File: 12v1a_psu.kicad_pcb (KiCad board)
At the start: 2 copper layers, 130 x 100 mm, 24 parts, among them J1 AC_in, J2 P1, J3 P2, J4 Vout, Q1 BD440, SW1 SW_SPST, U1 LM7812

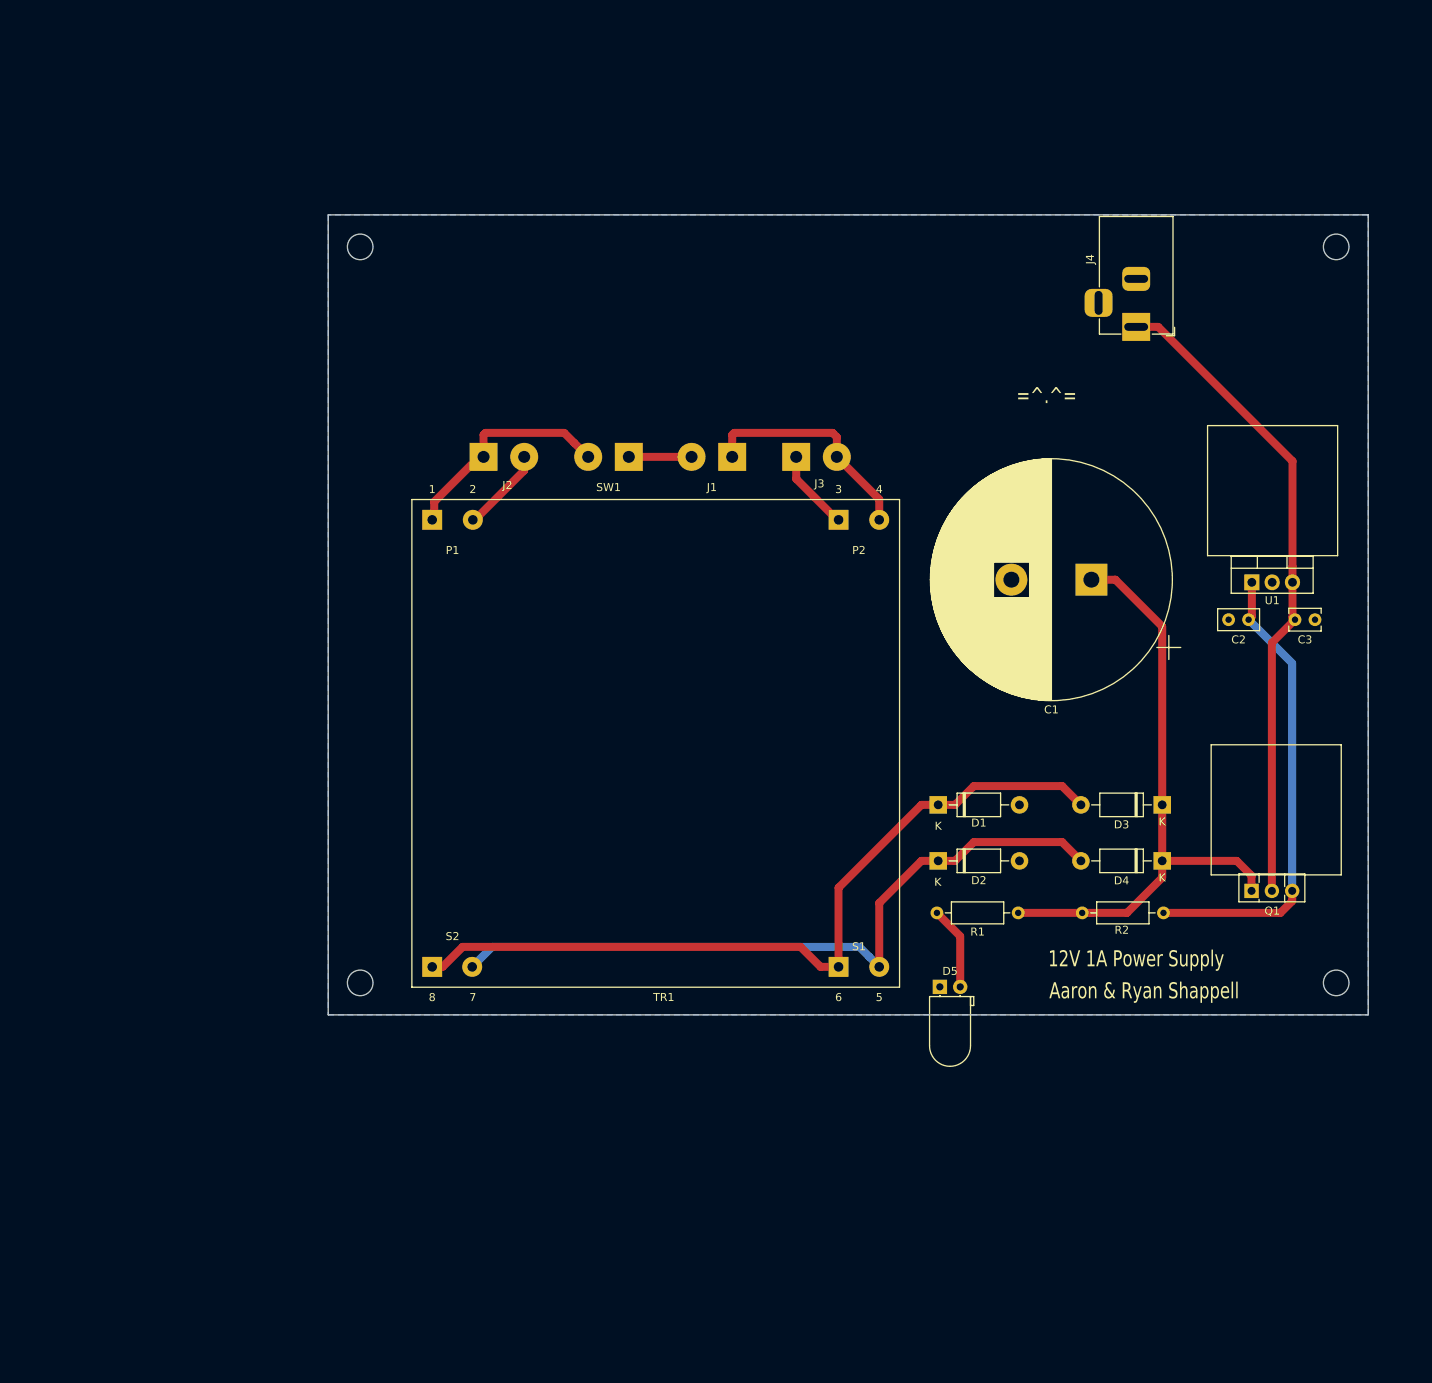
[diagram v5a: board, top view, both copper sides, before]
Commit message: Chose bjt for reg, picked footprints
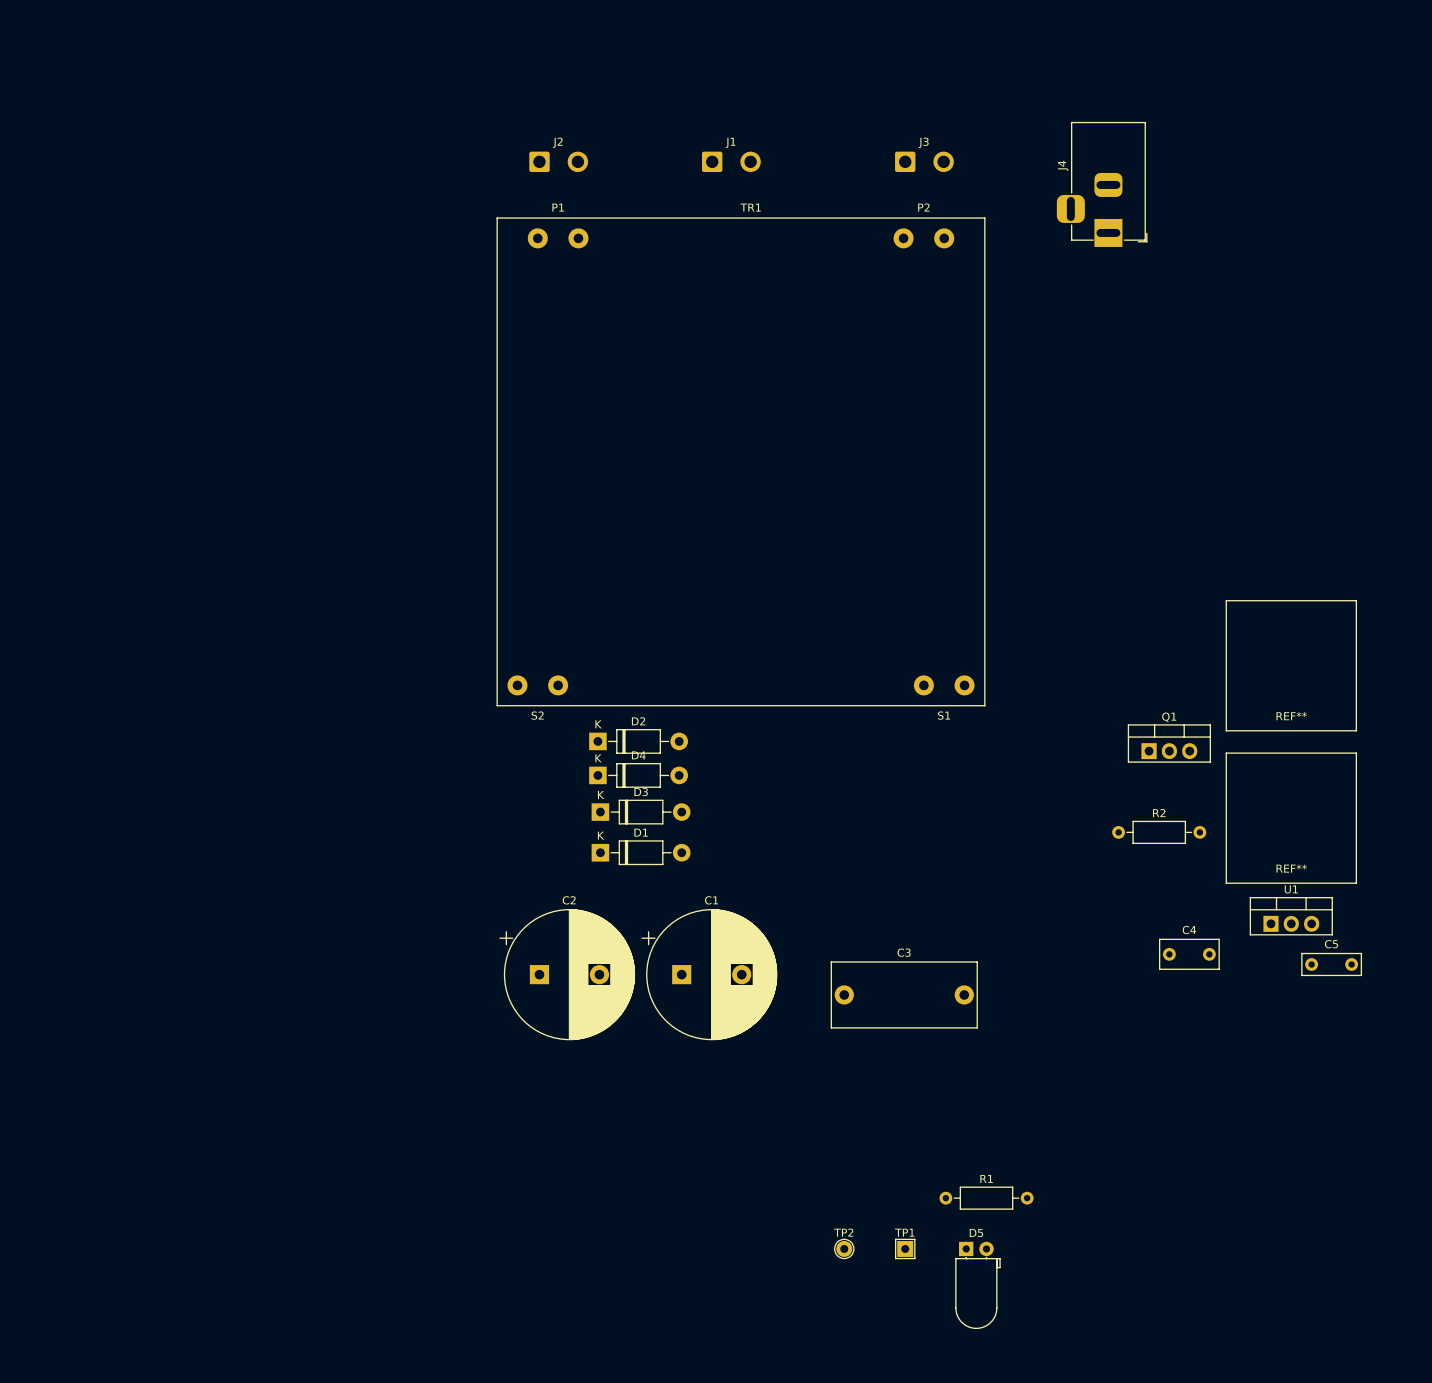
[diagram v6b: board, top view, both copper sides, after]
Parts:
- removed the REF** at (83.0, 142.0)
- removed the REF** at (205.0, 50.0)
- removed the REF** at (205.0, 142.0)
- removed the REF** at (83.0, 50.0)
- removed the REF** at (197.1, 88.6)
- removed the REF** at (197.5, 128.5)
- removed SW1: SW_SPST, Connector_Wire:SolderWirePad_1x02_P5.08mm_Drill1.5mm
- added C4: 0.33u, Capacitor_THT:C_Rect_L7.2mm_W3.5mm_P5.00mm_FKS2_FKP2_MKS2_MKP2, F.Cu at (184.2, 138.4)
- added C5: 0.1u, Capacitor_THT:C_Rect_L7.2mm_W2.5mm_P5.00mm_FKS2_FKP2_MKS2_MKP2, F.Cu at (201.9, 139.7)
- added REF**: Heatsink, 12v1a_psu:Heatsink, F.Cu at (199.4, 129.5)
- added REF**: Heatsink, 12v1a_psu:Heatsink, F.Cu at (199.4, 110.5)
- added TP1: TestPoint, TestPoint:TestPoint_THTPad_2.0x2.0mm_Drill1.0mm, F.Cu at (151.1, 175.3)
- added TP2: TestPoint, TestPoint:TestPoint_THTPad_D2.0mm_Drill1.0mm, F.Cu at (143.5, 175.3)
- C1: value 10000u -> 2200u; footprint Capacitor_THT:CP_Radial_D30.0mm_P10.00mm_SnapIn -> Capacitor_THT:CP_Radial_D16.0mm_P7.50mm
- C2: value 0.33u -> 2200u; footprint Capacitor_THT:C_Disc_D5.0mm_W2.5mm_P2.50mm -> Capacitor_THT:CP_Radial_D16.0mm_P7.50mm
- C3: value 0.1u -> 1u; footprint Capacitor_THT:C_Disc_D3.8mm_W2.6mm_P2.50mm -> Capacitor_THT:C_Rect_L18.0mm_W8.0mm_P15.00mm_FKS3_FKP3
- J1: value AC_in -> AC_IN; footprint Connector_Wire:SolderWirePad_1x02_P5.08mm_Drill1.5mm -> Connector_Wire:SolderWire-0.75sqmm_1x02_P4.8mm_D1.25mm_OD2.3mm
- J2, J3: footprint Connector_Wire:SolderWirePad_1x02_P5.08mm_Drill1.5mm -> Connector_Wire:SolderWire-0.75sqmm_1x02_P4.8mm_D1.25mm_OD2.3mm
- J4: footprint Connector_BarrelJack:BarrelJack_Horizontal -> 12v1a_psu:BarrelJack_Horizontal
- Q1: value BD440 -> TIP32AG; footprint Package_TO_SOT_THT:TO-126-3_Vertical -> Package_TO_SOT_THT:TO-220-3_Vertical
- TR1: footprint L01-6353:Transformer_L01-6353 -> 12v1a_psu:L01-6363
- U1: value LM7812 -> L7812
- moved C2 99.1 mm to (105.4, 141.0), turned to 0 degrees
- moved TR1 74.0 mm to (130.6, 76.9)
- moved C3 73.3 mm to (143.5, 143.5)
- moved D4 71.3 mm to (112.7, 116.1), turned to 0 degrees
- moved C1 71.1 mm to (123.2, 141.0), turned to 0 degrees
- moved D3 70.2 mm to (113.0, 120.7), turned to 0 degrees
- moved D2 45.1 mm to (112.7, 111.8)
- moved U1 42.8 mm to (196.8, 134.6)
- moved D1 42.6 mm to (113.0, 125.7)
- moved J3 39.3 mm to (151.1, 39.4)
- moved J2 37.5 mm to (105.4, 39.4)
- moved J1 37.0 mm to (127.0, 39.4), turned to 0 degrees
- moved R1 36.8 mm to (156.2, 168.9), turned to 0 degrees
- moved D5 32.9 mm to (158.8, 175.3)
- moved Q1 21.7 mm to (181.6, 113.0)
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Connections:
- net Net-(J1-Pad1) renamed /AC_N
- C2 pad 1: Net-(C2-Pad1) -> Net-(C1-Pad1)
- C3 pad 1: Net-(C3-Pad1) -> Net-(C1-Pad1)
- J1 pad 2: Net-(J1-Pad2) -> /AC_L
- J2 pad 1: Net-(J2-Pad1) -> /AC_L
- J4 pad 1: Net-(C3-Pad1) -> +12V
- Q1 pad 1: Net-(C1-Pad1) -> Net-(C4-Pad1)
- Q1 pad 2: Net-(C3-Pad1) -> +12V
- Q1 pad 3: Net-(C2-Pad1) -> Net-(C1-Pad1)
- R2 pad 1: Net-(C1-Pad1) -> Net-(C4-Pad1)
- R2 pad 2: Net-(C2-Pad1) -> Net-(C1-Pad1)
- TR1 pad 1: Net-(J2-Pad1) -> /AC_L
- U1 pad 1: Net-(C2-Pad1) -> Net-(C4-Pad1)
- U1 pad 3: Net-(C3-Pad1) -> +12V
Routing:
- net /S1P: track 99.3 -> 0.00 mm
- net /S1N: track 90.3 -> 0.00 mm
- net Net-(C3-Pad1): track 81.5 -> 0.00 mm
- net Net-(C1-Pad1): track 76.3 -> 0.00 mm
- net Net-(C2-Pad1): track 59.0 -> 0.00 mm
- net /AC_N: track 28.7 -> 0.00 mm
- net Net-(J2-Pad1): track 28.6 -> 0.00 mm
- net Net-(D5-Pad2): track 10.5 -> 0.00 mm
- net Net-(J2-Pad2): track 10.4 -> 0.00 mm
- net Net-(J3-Pad1): track 10.4 -> 0.00 mm
- net Net-(J1-Pad2): track 7.84 -> 0.00 mm
- removed copper zone on B.Cu, net GND
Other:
- board outline removed
- board text removed: "12V 1A Power Supply"
- board text removed: "=^.^="
- board text removed: "Aaron & Ryan Shappell"

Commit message: Add parts list, add case and ac receptable step files
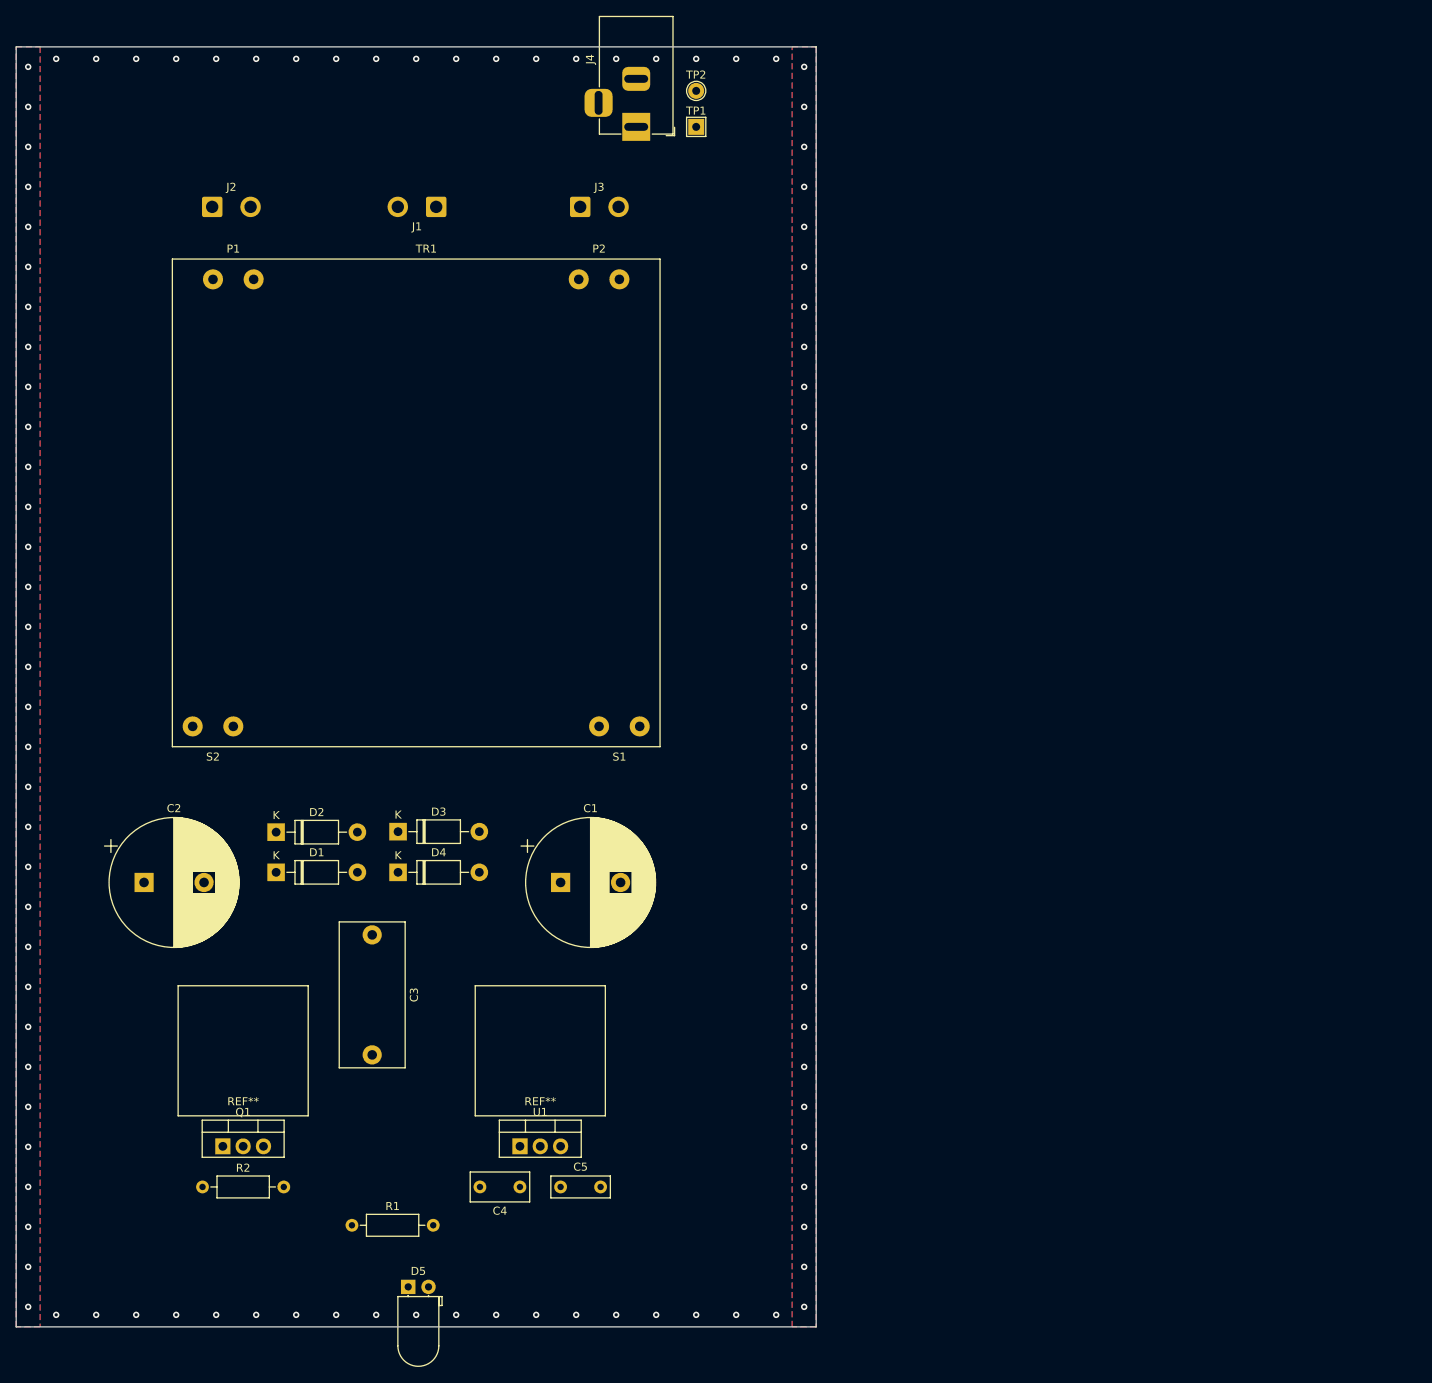
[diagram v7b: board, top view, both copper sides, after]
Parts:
- moved TP2 145.9 mm to (125.0, 30.5)
- moved TP1 142.7 mm to (125.0, 35.0)
- moved REF** 139.6 mm to (68.4, 158.6)
- moved Q1 125.9 mm to (65.8, 162.4)
- moved R2 122.8 mm to (63.3, 167.5)
- moved REF** 98.3 mm to (105.5, 158.6)
- moved C5 97.9 mm to (108.0, 167.5)
- moved U1 97.9 mm to (103.0, 162.4)
- moved C4 86.2 mm to (103.0, 167.5), turned to 180 degrees
- moved R1 74.3 mm to (82.0, 172.3)
- moved D5 69.9 mm to (89.0, 180.0)
- moved J4 60.5 mm to (117.5, 35.0)
- moved C3 59.5 mm to (84.5, 136.0), turned to 270 degrees
- moved C2 50.8 mm to (56.0, 129.4)
- moved D2 41.8 mm to (72.5, 123.2)
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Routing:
- net GND: vias 0 -> 102
- added copper zone on PWR.Cu, net +12V
- added copper zone on B.Cu, net GND
- added copper zone on F.Cu, net GND
- added copper zone on GND.Cu, net GND
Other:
- board outline added: 100 x 160 mm
- copper layers 2 -> 4
- net class Default: clearance 0.75 -> 0.8; trace_width 1 -> 0.5
- rule trace_clearance: 0.75 -> 0.8

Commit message: Component and trace layout
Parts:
- moved C1 51.8 mm to (69.0, 163.5), turned to 180 degrees
- moved Q1 50.4 mm to (114.0, 177.4)
- moved REF** 50.4 mm to (116.5, 173.6)
- moved R2 36.7 mm to (99.5, 161.5), turned to 180 degrees
- moved D2 31.2 mm to (103.2, 129.0), turned to 180 degrees
- moved C3 25.8 mm to (80.5, 161.5), turned to 90 degrees
- moved C2 19.5 mm to (69.0, 144.0), turned to 180 degrees
- moved D4 16.9 mm to (103.2, 135.0), turned to 180 degrees
- moved D3 16.1 mm to (76.8, 135.0)
- moved REF** 13.9 mm to (116.5, 150.1)
- moved U1 13.9 mm to (114.0, 153.9)
- moved R1 13.7 mm to (95.5, 174.5), turned to 180 degrees
- moved C4 13.5 mm to (103.0, 154.0), turned to 90 degrees
- moved J1 12.8 mm to (92.5, 57.8)
- moved J2 12.8 mm to (64.5, 57.8)
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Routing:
- net Net-(C1-Pad1): track 0.00 -> 129.5 mm
- net /S1N: track 0.00 -> 83.9 mm
- net /S1P: track 0.00 -> 69.8 mm
- net Net-(C4-Pad1): track 0.00 -> 43.5 mm
- net /AC_L: track 0.00 -> 36.4 mm
- net /AC_N: track 0.00 -> 36.0 mm
- net Net-(D5-Pad2): track 0.00 -> 9.22 mm
- net Net-(J2-Pad2): track 0.00 -> 9.22 mm
- net Net-(J3-Pad1): track 0.00 -> 9.13 mm
